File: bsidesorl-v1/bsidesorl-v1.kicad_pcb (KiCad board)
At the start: 2 copper layers, 97.8 x 92.6 mm, 15 parts, among them SW1 MST22D18G2 125

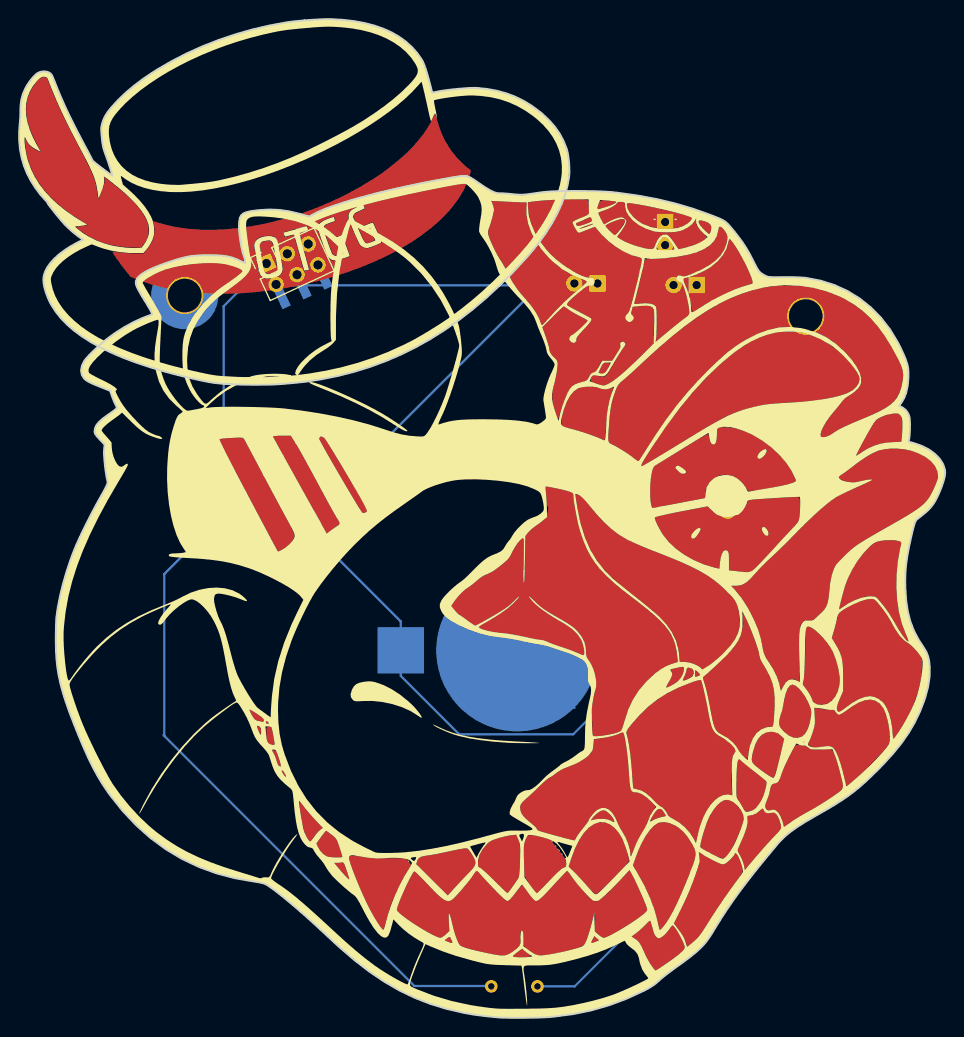
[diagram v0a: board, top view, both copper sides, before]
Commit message: introduced additional sao
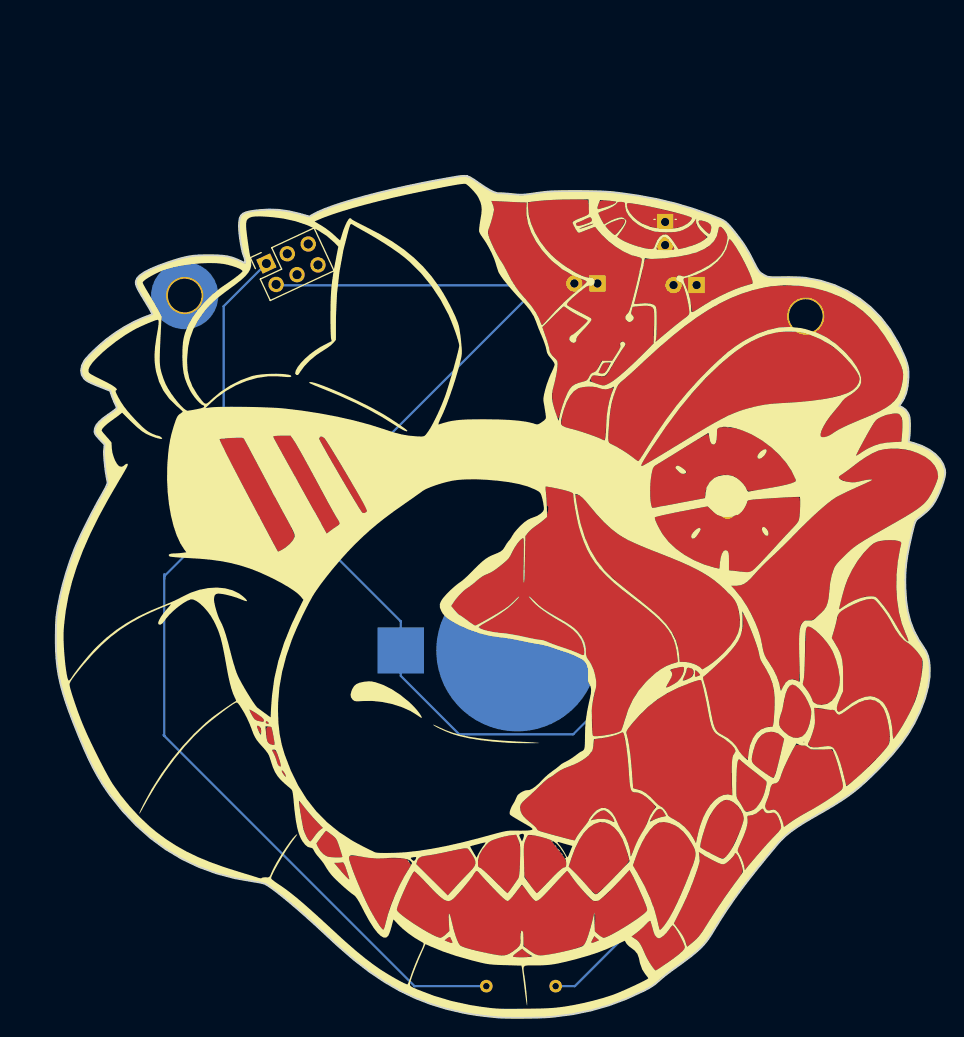
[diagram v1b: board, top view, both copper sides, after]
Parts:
- removed the G*** at (127.7, 58.2)
- removed the SAO at (127.1, 65.2)
- R1: footprint Resistor_THT:R_Axial_DIN0204_L3.6mm_D1.6mm_P5.08mm_Vertical -> Resistor_THT:R_Axial_DIN0204_L3.6mm_D1.6mm_P7.62mm_Horizontal
- moved R1 2.00 mm to (156.0, 144.5)
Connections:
- SW1 pad 2: unconnected-(SW1-Pad2) -> Net-(BT1-+)
- SW1 pad 6: unconnected-(SW1-Pad6) -> Net-(D2-A)
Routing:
- net Net-(D2-A): track 168.3 -> 179.2 mm
- net Net-(BT1--): track 118.6 -> 109.6 mm
- net Net-(BT1-+): track 55.8 -> 61.6 mm
- net Net-(D1-A): track 63.4 -> 61.4 mm
